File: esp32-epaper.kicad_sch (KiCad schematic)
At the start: 52 parts, among them J1 USB-C 16P, J2 FPC-26P, J3 PH2.0 2P Battery, Q1 AO3400A, SW1 SW SPDT, U1 ESP32-WROOM-32D, U2 SSD1680, U3 TP4056, U4 DW01A, U5 FS8205A, U6 HT7333-1

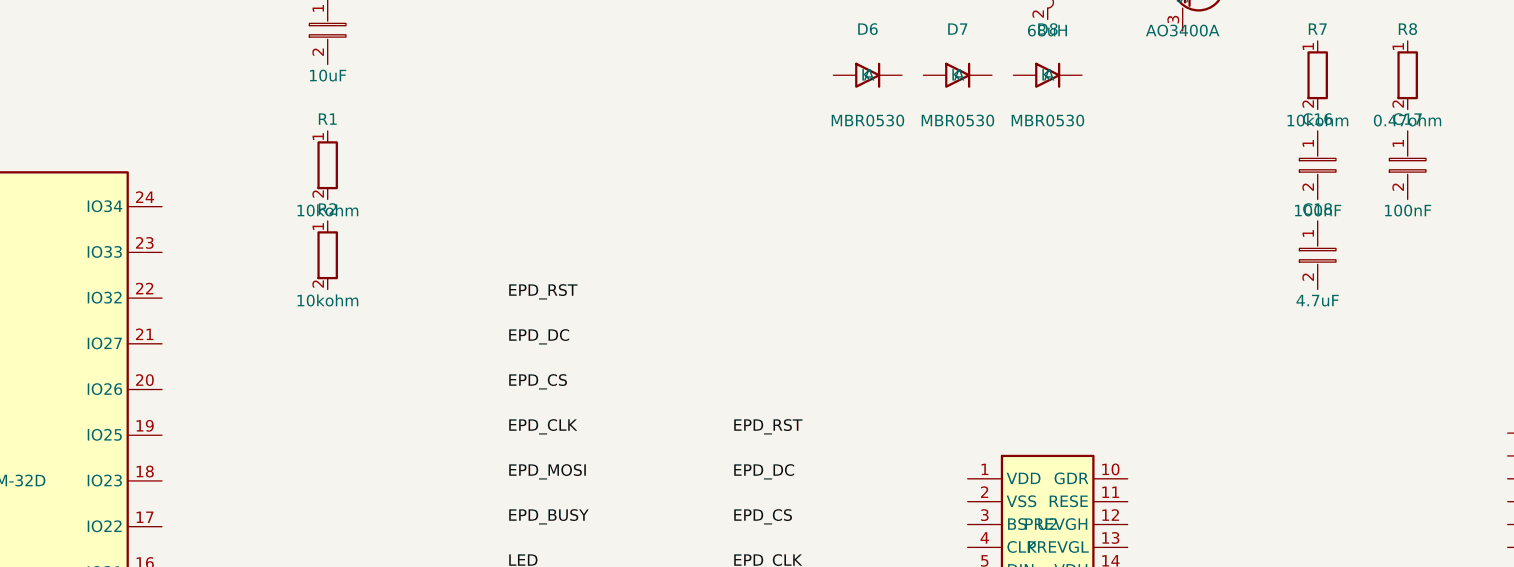
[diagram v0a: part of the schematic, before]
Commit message: feat: add next-pcb user provisioning button
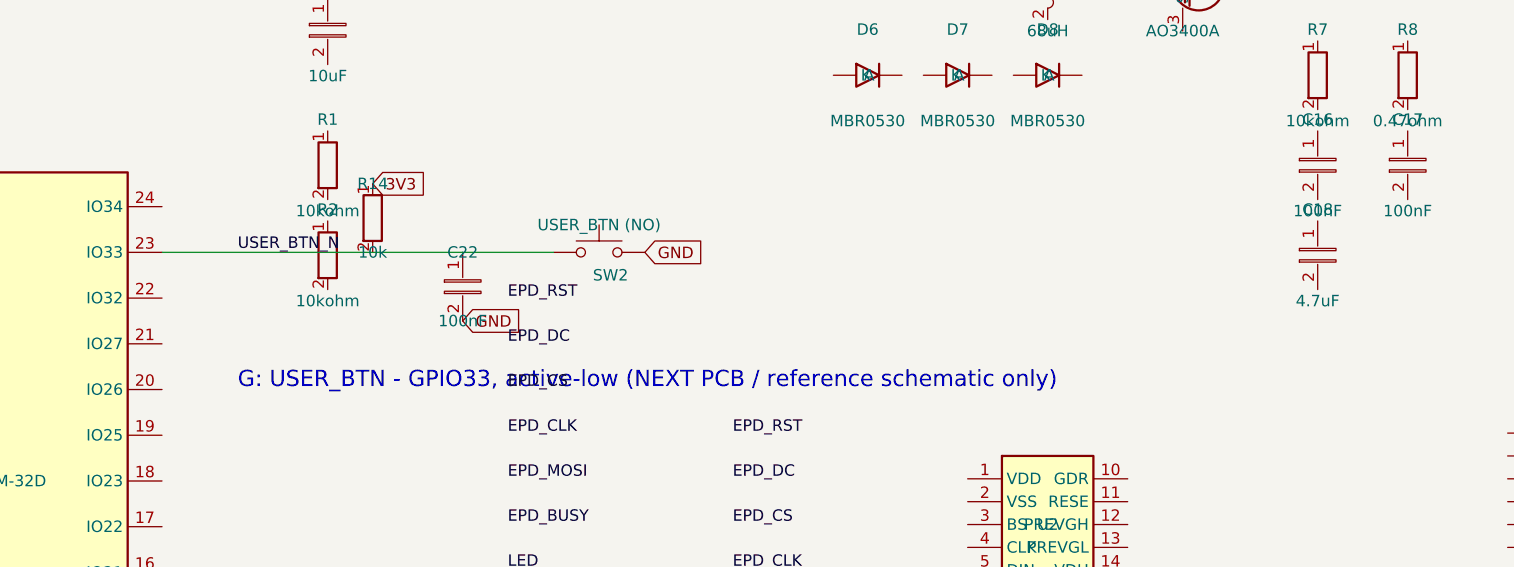
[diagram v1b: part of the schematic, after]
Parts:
- added C22: 100nF, Capacitor_SMD:C_0603_1608Metric, symbol Device:C
- added R14: 10k, Resistor_SMD:R_0603_1608Metric, symbol Device:R
- added SW2: USER_BTN (NO), Button_Switch_SMD:SW_SPST_TL3301AN, symbol Switch:SW_Push
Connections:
- net 3V3: now also R14.1
- net GND: now also C22.2, SW2.2
- net USER_BTN_N: now reaches U1.23 (IO33)
- net USER_BTN_N: now also C22.1, R14.2, SW2.1
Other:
- note added: "G: USER_BTN - GPIO33, active-low (NEXT PCB / reference schematic only)"
- title: ESP32 E-Paper Badge v1.1 -> ESP32 E-Paper Badge v1.2
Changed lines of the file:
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@@
   (paper "A3" portrait)
   (title_block
-    (title "ESP32 E-Paper Badge v1.1")
-    (date "2026-06-04")
-    (rev "1.1")
+    (title "ESP32 E-Paper Badge v1.2")
+    (date "2026-08-22")
+    (rev "1.2")
     (company "LuckyDog")
     (comment 1 "ESP32-WROOM-32D + SSD1680 + TP4056 + HT7333")
     (comment 2 "2.13\" Tri-color E-Paper, USB-C Charging + USB Direct Power")
   )
+  (text "G: USER_BTN - GPIO33, active-low (NEXT PCB / reference schematic only)" (at 105 60 0)
+    (effects (font (size 1.8 1.8)) (justify left bottom))
+  )
   (text "F: USB/Battery Power Path - D3/D4 SS14 OR-ing + J3 PH2.0" (at 100 228 0)
     (effects (font (size 2.54 2.54)) (justify left bottom))
@@
     (effects (font (size 2.54 2.54)) (justify left bottom))
   )
+  (wire (pts (xy 96.59 44.68) (xy 120 44.68))
+    (stroke (width 0) (type default))
+  )
+  (wire (pts (xy 120 44.68) (xy 130 44.68))
+    (stroke (width 0) (type default))
+  )
+  (wire (pts (xy 130 44.68) (xy 140.08 44.68))
+    (stroke (width 0) (type default))
+  )
   (wire (pts (xy 105 235) (xy 130 235))
     (stroke (width 0) (type default))
@@
     (stroke (width 0) (type default))
   )
+  (global_label "3V3" (shape input) (at 120 37.06 0) (fields_autoplaced)
+    (effects (font (size 1.27 1.27)) (justify left))
+  )
+  (global_label "GND" (shape input) (at 130 52.3 0) (fields_autoplaced)
+    (effects (font (size 1.27 1.27)) (justify left))
+  )
+  (global_label "GND" (shape input) (at 150.24 44.68 0) (fields_autoplaced)
+    (effects (font (size 1.27 1.27)) (justify left))
+  )
+  (label "USER_BTN_N" (at 105 44.68 0)
+    (effects (font (size 1.27 1.27)) (justify left bottom))
+  )
   (global_label "VBUS" (shape input) (at 105 230 0) (fields_autoplaced)
     (effects (font (size 1.27 1.27)) (justify left))
@@
   (label "LED" (at 245 250 0)
     (effects (font (size 1.27 1.27)) (justify left bottom))
+  )
+  (symbol (lib_id "Device:R") (at 120 40.87 0) (unit 1)
+    (in_bom yes) (on_board yes) (dnp no)
+    (property "Reference" "R14" (at 120 37.06 0)
+      (effects (font (size 1.27 1.27)))
+    )
+    (property "Value" "10k" (at 120 44.68 0)
+      (effects (font (size 1.27 1.27)))
+    )
+    (property "Footprint" "Resistor_SMD:R_0603_1608Metric" (at 120 40.87 0)
+      (effects (font (size 1.27 1.27)) hide)
+    )
+    (pin "1")
+    (pin "2")
+    (instances
+      (project "esp32-epaper"
+        (path "/6281fcfa-6553-4706-b287-236232e6465c"
+          (reference "R14") (unit 1)
+        )
+      )
+    )
+  )
+  (symbol (lib_id "Device:C") (at 130 48.49 0) (unit 1)
+    (in_bom yes) (on_board yes) (dnp no)
+    (property "Reference" "C22" (at 130 44.68 0)
+      (effects (font (size 1.27 1.27)))
+    )
+    (property "Value" "100nF" (at 130 52.3 0)
+      (effects (font (size 1.27 1.27)))
+    )
+    (property "Footprint" "Capacitor_SMD:C_0603_1608Metric" (at 130 48.49 0)
+      (effects (font (size 1.27 1.27)) hide)
+    )
+    (pin "1")
+    (pin "2")
+    (instances
+      (project "esp32-epaper"
+        (path "/6281fcfa-6553-4706-b287-236232e6465c"
+          (reference "C22") (unit 1)
+        )
+      )
+    )
+  )
+  (symbol (lib_id "Switch:SW_Push") (at 145.16 44.68 0) (unit 1)
+    (in_bom yes) (on_board yes) (dnp no)
+    (property "Reference" "SW2" (at 146.43 47.22 0)
+      (effects (font (size 1.27 1.27)))
+    )
+    (property "Value" "USER_BTN (NO)" (at 145.16 41.632 0)
+      (effects (font (size 1.27 1.27)))
+    )
+    (property "Footprint" "Button_Switch_SMD:SW_SPST_TL3301AN" (at 145.16 44.68 0)
+      (effects (font (size 1.27 1.27)) hide)
+    )
+    (pin "1")
+    (pin "2")
+    (instances
+      (project "esp32-epaper"
+        (path "/6281fcfa-6553-4706-b287-236232e6465c"
+          (reference "SW2") (unit 1)
+        )
+      )
+    )
   )
   (symbol (lib_id "RF_Module:ESP32-WROOM-32D") (at 75 65 0) (unit 1)
@@
     (path "/6281fcfa-6553-4706-b287-236232e6465c/ef915b23-cd38-459e-98a6-52f5482c4f7d" (reference "D5") (unit 1) (value "Green") (footprint ""))
     (path "/6281fcfa-6553-4706-b287-236232e6465c/531d4d44-7088-4b86-a585-529e39b7fbe9" (reference "R11") (unit 1) (value "1kohm") (footprint ""))
+    (path "/6281fcfa-6553-4706-b287-236232e6465c/0dd9dc0d-8963-4a01-942c-5410becc1dc0" (reference "R14") (unit 1) (value "10k") (footprint "Resistor_SMD:R_0603_1608Metric"))
+    (path "/6281fcfa-6553-4706-b287-236232e6465c/b25f8a6b-1b70-4fde-bf80-dc818a410306" (reference "C22") (unit 1) (value "100nF") (footprint "Capacitor_SMD:C_0603_1608Metric"))
+    (path "/6281fcfa-6553-4706-b287-236232e6465c/1d5a7f72-ee96-4a89-b7f5-5f4c693fb09e" (reference "SW2") (unit 1) (value "USER_BTN (NO)") (footprint "Button_Switch_SMD:SW_SPST_TL3301AN"))
   )
 )
